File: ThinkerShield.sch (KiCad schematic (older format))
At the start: 36 parts, among them SW1 SW_PUSHBUTTON, SW2 SW_PUSHBUTTON, U1 BUZZER

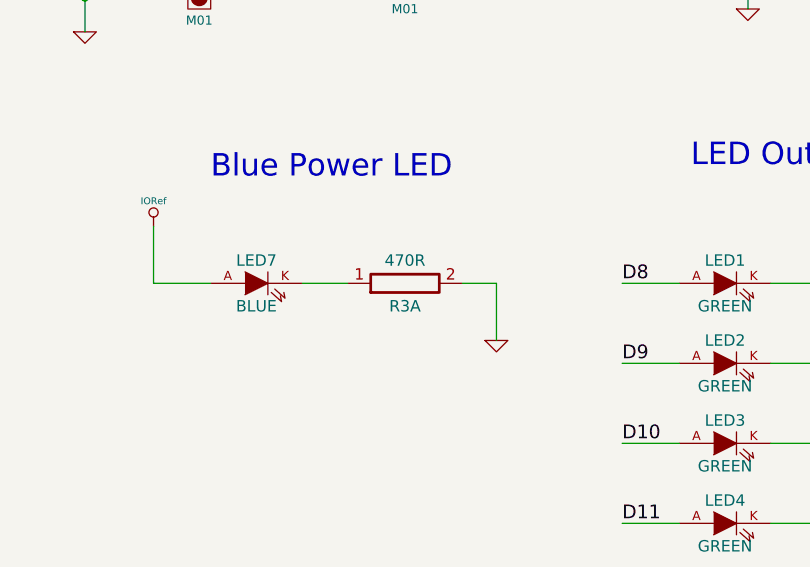
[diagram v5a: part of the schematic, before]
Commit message: Spread out LEDs, use better MAAS logo
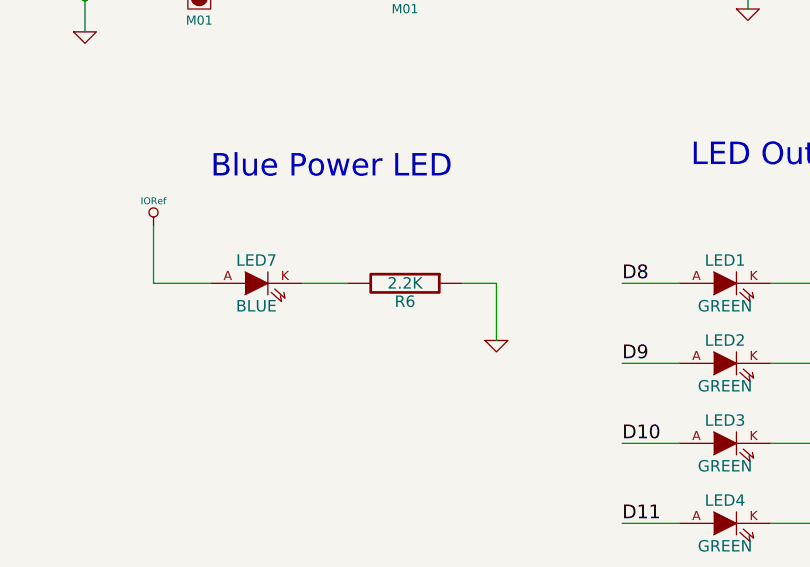
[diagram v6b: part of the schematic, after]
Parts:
- removed unit 1 of R3
- added R6: 2.2K, FT:0603, symbol R
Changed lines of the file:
@@
 EESchema Schematic File Version 2
+LIBS:ThinkerShield-rescue
 LIBS:freetronics_schematic
 LIBS:power
@@
 LIBS:memory
 LIBS:xilinx
-LIBS:special
 LIBS:microcontrollers
 LIBS:dsp
@@
 $EndComp
 $Comp
-L GND #PWR01
+L GND-RESCUE-ThinkerShield #PWR01
 U 1 1 5488FE79
 P 9650 6050
@@
 $EndComp
 $Comp
-L GND #PWR02
+L GND-RESCUE-ThinkerShield #PWR02
 U 1 1 54890309
 P 1300 3500
@@
 $EndComp
 $Comp
-L GND #PWR06
+L GND-RESCUE-ThinkerShield #PWR06
 U 1 1 5489283C
 P 5800 2950
@@
 NoConn ~ 4450 5000
 $Comp
-L GND #PWR08
+L GND-RESCUE-ThinkerShield #PWR08
 U 1 1 54894485
 P 4900 5850
@@
 $EndComp
 $Comp
-L GND #PWR09
+L GND-RESCUE-ThinkerShield #PWR09
 U 1 1 54894A14
 P 1950 6500
@@
 F 3 "" H 9250 4750 60  0000 C CNN
 	4    9250 4750
-	1    0    0    -1
-$EndComp
-$Comp
-L R_PACK4_IND R4
-U 1 1 54896064
-P 9250 5100
-F 0 "R4" H 9250 5000 50  0000 C CNN
-F 1 "470R" H 9250 5200 50  0000 C CNN
-F 2 "FT:RES_CAY16" H 9250 4950 39  0001 C CNN
-F 3 "" H 9250 5100 60  0000 C CNN
-	1    9250 5100
 	1    0    0    -1
 $EndComp
@@
 	10250 4650 10250 5800
 $Comp
-L GND #PWR011
+L GND-RESCUE-ThinkerShield #PWR011
 U 1 1 5489A66F
 P 10250 5800
@@
 	1500 6000 1500 6150
 $Comp
-L GND #PWR012
+L GND-RESCUE-ThinkerShield #PWR012
 U 1 1 5489CC22
 P 1500 7000
@@
 $EndComp
 $Comp
-L GND #PWR015
+L GND-RESCUE-ThinkerShield #PWR015
 U 1 1 5489E9C2
 P 2150 3500
@@
 $EndComp
 $Comp
-L GND #PWR016
+L GND-RESCUE-ThinkerShield #PWR016
 U 1 1 5489EAC4
 P 3050 3500
@@
 	8700 2750 8700 2850
 $Comp
-L GND #PWR017
+L GND-RESCUE-ThinkerShield #PWR017
 U 1 1 548A6BBB
 P 8700 2850
@@
 $EndComp
 $Comp
-L GND #PWR018
+L GND-RESCUE-ThinkerShield #PWR018
 U 1 1 548A6CBD
 P 9800 2850
@@
 Wire Wire Line
 	7450 4050 7600 4050
+Wire Wire Line
+	6100 4050 6100 3800
+$Comp
+L IORef #PWR021
+U 1 1 556FE007
+P 6100 3800
+F 0 "#PWR021" H 6100 3760 30  0001 C CNN
+F 1 "IORef" H 6100 3910 30  0000 C CNN
+F 2 "" H 6100 3800 60  0000 C CNN
+F 3 "" H 6100 3800 60  0000 C CNN
+	1    6100 3800
+	1    0    0    -1
+$EndComp
+Wire Wire Line
+	7600 4050 7600 4300
+$Comp
+L GND-RESCUE-ThinkerShield #PWR022
+U 1 1 556FE611
+P 7600 4300
+F 0 "#PWR022" H 7600 4300 30  0001 C CNN
+F 1 "GND" H 7600 4230 30  0001 C CNN
+F 2 "" H 7600 4300 60  0000 C CNN
+F 3 "" H 7600 4300 60  0000 C CNN
+	1    7600 4300
+	1    0    0    -1
+$EndComp
+Text Notes 6350 3600 0    98   ~ 0
+Blue Power LED\n
+$Comp
+L R_PACK4_IND R4
+U 3 1 556FC554
+P 9250 5800
+F 0 "R4" H 9250 5700 50  0000 C CNN
+F 1 "470R" H 9250 5900 50  0000 C CNN
+F 2 "FT:RES_CAY16" H 9250 5650 39  0001 C CNN
+F 3 "" H 9250 5800 60  0000 C CNN
+	3    9250 5800
+	1    0    0    -1
+$EndComp
 $Comp
 L R_PACK4_IND R4
@@
 $Comp
 L R_PACK4_IND R4
-U 3 1 556FC554
-P 9250 5800
-F 0 "R4" H 9250 5700 50  0000 C CNN
-F 1 "470R" H 9250 5900 50  0000 C CNN
-F 2 "FT:RES_CAY16" H 9250 5650 39  0001 C CNN
-F 3 "" H 9250 5800 60  0000 C CNN
-	3    9250 5800
-	1    0    0    -1
-$EndComp
-$Comp
-L R_PACK4_IND R3
-U 1 1 556FC603
+U 1 1 54896064
+P 9250 5100
+F 0 "R4" H 9250 5000 50  0000 C CNN
+F 1 "470R" H 9250 5200 50  0000 C CNN
+F 2 "FT:RES_CAY16" H 9250 4950 39  0001 C CNN
+F 3 "" H 9250 5100 60  0000 C CNN
+	1    9250 5100
+	1    0    0    -1
+$EndComp
+$Comp
+L R R6
+U 1 1 55BEC76A
 P 7200 4050
-F 0 "R3" H 7200 3950 50  0000 C CNN
-F 1 "470R" H 7200 4150 50  0000 C CNN
-F 2 "FT:RES_CAY16" H 7200 3900 39  0001 C CNN
+F 0 "R6" V 7280 4050 50  0000 C CNN
+F 1 "2.2K" V 7200 4050 50  0000 C CNN
+F 2 "FT:0603" H 7200 4050 60  0001 C CNN
 F 3 "" H 7200 4050 60  0000 C CNN
 	1    7200 4050
-	1    0    0    -1
-$EndComp
-Wire Wire Line
-	6100 4050 6100 3800
-$Comp
-L IORef #PWR021
-U 1 1 556FE007
-P 6100 3800
-F 0 "#PWR021" H 6100 3760 30  0001 C CNN
-F 1 "IORef" H 6100 3910 30  0000 C CNN
-F 2 "" H 6100 3800 60  0000 C CNN
-F 3 "" H 6100 3800 60  0000 C CNN
-	1    6100 3800
-	1    0    0    -1
-$EndComp
-Wire Wire Line
-	7600 4050 7600 4300
-$Comp
-L GND #PWR022
-U 1 1 556FE611
-P 7600 4300
-F 0 "#PWR022" H 7600 4300 30  0001 C CNN
-F 1 "GND" H 7600 4230 30  0001 C CNN
-F 2 "" H 7600 4300 60  0000 C CNN
-F 3 "" H 7600 4300 60  0000 C CNN
-	1    7600 4300
-	1    0    0    -1
-$EndComp
-Text Notes 6350 3600 0    98   ~ 0
-Blue Power LED\n
+	0    1    1    0
+$EndComp
 $EndSCHEMATC

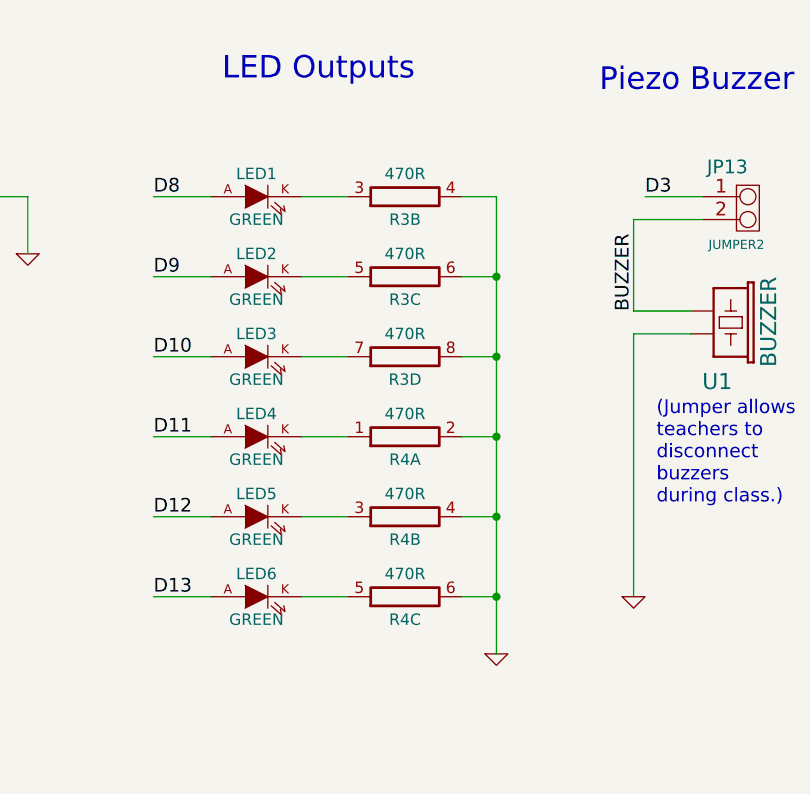
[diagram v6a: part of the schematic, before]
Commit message: Split resistor packs into individual resistors, spread LEDs out some more
Also includes upgrade to KiCad 2015-08 which no longer uses .cmp files
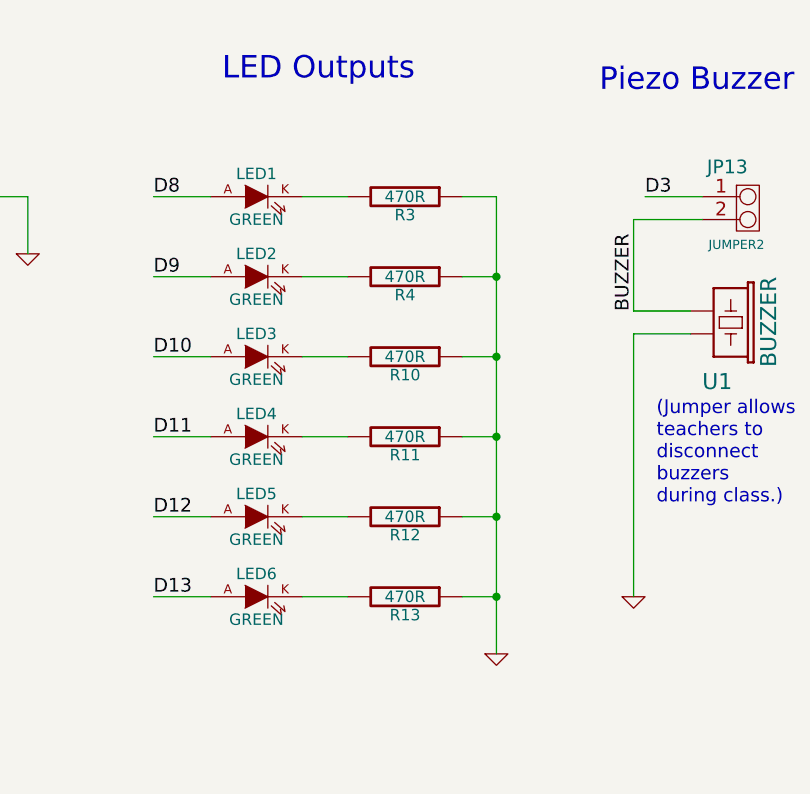
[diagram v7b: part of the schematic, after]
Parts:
- removed R3, R4: 470R, FT:RES_CAY16, symbol R_PACK4_IND
- added R10, R11, R12, R13, R3, R4: 470R, FT:0603, symbol R
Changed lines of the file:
@@
 Arduino Shield Header
-$Comp
-L R_PACK4_IND R3
-U 2 1 54895F4D
-P 9250 4050
-F 0 "R3" H 9250 3950 50  0000 C CNN
-F 1 "470R" H 9250 4150 50  0000 C CNN
-F 2 "FT:RES_CAY16" H 9250 3900 39  0001 C CNN
-F 3 "" H 9250 4050 60  0000 C CNN
-	2    9250 4050
-	1    0    0    -1
-$EndComp
-$Comp
-L R_PACK4_IND R3
-U 3 1 54895FDF
-P 9250 4400
-F 0 "R3" H 9250 4300 50  0000 C CNN
-F 1 "470R" H 9250 4500 50  0000 C CNN
-F 2 "FT:RES_CAY16" H 9250 4250 39  0001 C CNN
-F 3 "" H 9250 4400 60  0000 C CNN
-	3    9250 4400
-	1    0    0    -1
-$EndComp
-$Comp
-L R_PACK4_IND R3
-U 4 1 5489601F
-P 9250 4750
-F 0 "R3" H 9250 4650 50  0000 C CNN
-F 1 "470R" H 9250 4850 50  0000 C CNN
-F 2 "FT:RES_CAY16" H 9250 4600 39  0001 C CNN
-F 3 "" H 9250 4750 60  0000 C CNN
-	4    9250 4750
-	1    0    0    -1
-$EndComp
 $Comp
 L +5V #PWR010
@@
 Blue Power LED\n
 $Comp
-L R_PACK4_IND R4
-U 3 1 556FC554
-P 9250 5800
-F 0 "R4" H 9250 5700 50  0000 C CNN
-F 1 "470R" H 9250 5900 50  0000 C CNN
-F 2 "FT:RES_CAY16" H 9250 5650 39  0001 C CNN
-F 3 "" H 9250 5800 60  0000 C CNN
-	3    9250 5800
-	1    0    0    -1
-$EndComp
-$Comp
-L R_PACK4_IND R4
-U 2 1 556FC4AC
-P 9250 5450
-F 0 "R4" H 9250 5350 50  0000 C CNN
-F 1 "470R" H 9250 5550 50  0000 C CNN
-F 2 "FT:RES_CAY16" H 9250 5300 39  0001 C CNN
-F 3 "" H 9250 5450 60  0000 C CNN
-	2    9250 5450
-	1    0    0    -1
-$EndComp
-$Comp
-L R_PACK4_IND R4
-U 1 1 54896064
-P 9250 5100
-F 0 "R4" H 9250 5000 50  0000 C CNN
-F 1 "470R" H 9250 5200 50  0000 C CNN
-F 2 "FT:RES_CAY16" H 9250 4950 39  0001 C CNN
-F 3 "" H 9250 5100 60  0000 C CNN
-	1    9250 5100
-	1    0    0    -1
-$EndComp
-$Comp
 L R R6
 U 1 1 55BEC76A
@@
 	0    1    1    0
 $EndComp
+$Comp
+L R R3
+U 1 1 55DE6001
+P 9250 4050
+F 0 "R3" V 9330 4050 50  0000 C CNN
+F 1 "470R" V 9250 4050 50  0000 C CNN
+F 2 "FT:0603" H 9250 4050 60  0001 C CNN
+F 3 "" H 9250 4050 60  0000 C CNN
+	1    9250 4050
+	0    1    1    0
+$EndComp
+$Comp
+L R R4
+U 1 1 55DE6626
+P 9250 4400
+F 0 "R4" V 9330 4400 50  0000 C CNN
+F 1 "470R" V 9250 4400 50  0000 C CNN
+F 2 "FT:0603" H 9250 4400 60  0001 C CNN
+F 3 "" H 9250 4400 60  0000 C CNN
+	1    9250 4400
+	0    1    1    0
+$EndComp
+$Comp
+L R R10
+U 1 1 55DE66E8
+P 9250 4750
+F 0 "R10" V 9330 4750 50  0000 C CNN
+F 1 "470R" V 9250 4750 50  0000 C CNN
+F 2 "FT:0603" H 9250 4750 60  0001 C CNN
+F 3 "" H 9250 4750 60  0000 C CNN
+	1    9250 4750
+	0    1    1    0
+$EndComp
+$Comp
+L R R11
+U 1 1 55DE6A16
+P 9250 5100
+F 0 "R11" V 9330 5100 50  0000 C CNN
+F 1 "470R" V 9250 5100 50  0000 C CNN
+F 2 "FT:0603" H 9250 5100 60  0001 C CNN
+F 3 "" H 9250 5100 60  0000 C CNN
+	1    9250 5100
+	0    1    1    0
+$EndComp
+$Comp
+L R R12
+U 1 1 55DE6AD4
+P 9250 5450
+F 0 "R12" V 9330 5450 50  0000 C CNN
+F 1 "470R" V 9250 5450 50  0000 C CNN
+F 2 "FT:0603" H 9250 5450 60  0001 C CNN
+F 3 "" H 9250 5450 60  0000 C CNN
+	1    9250 5450
+	0    1    1    0
+$EndComp
+$Comp
+L R R13
+U 1 1 55DE6B94
+P 9250 5800
+F 0 "R13" V 9330 5800 50  0000 C CNN
+F 1 "470R" V 9250 5800 50  0000 C CNN
+F 2 "FT:0603" H 9250 5800 60  0001 C CNN
+F 3 "" H 9250 5800 60  0000 C CNN
+	1    9250 5800
+	0    1    1    0
+$EndComp
